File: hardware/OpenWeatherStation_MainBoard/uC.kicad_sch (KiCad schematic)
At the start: 1 part, among them U1 STM32F107VCTx

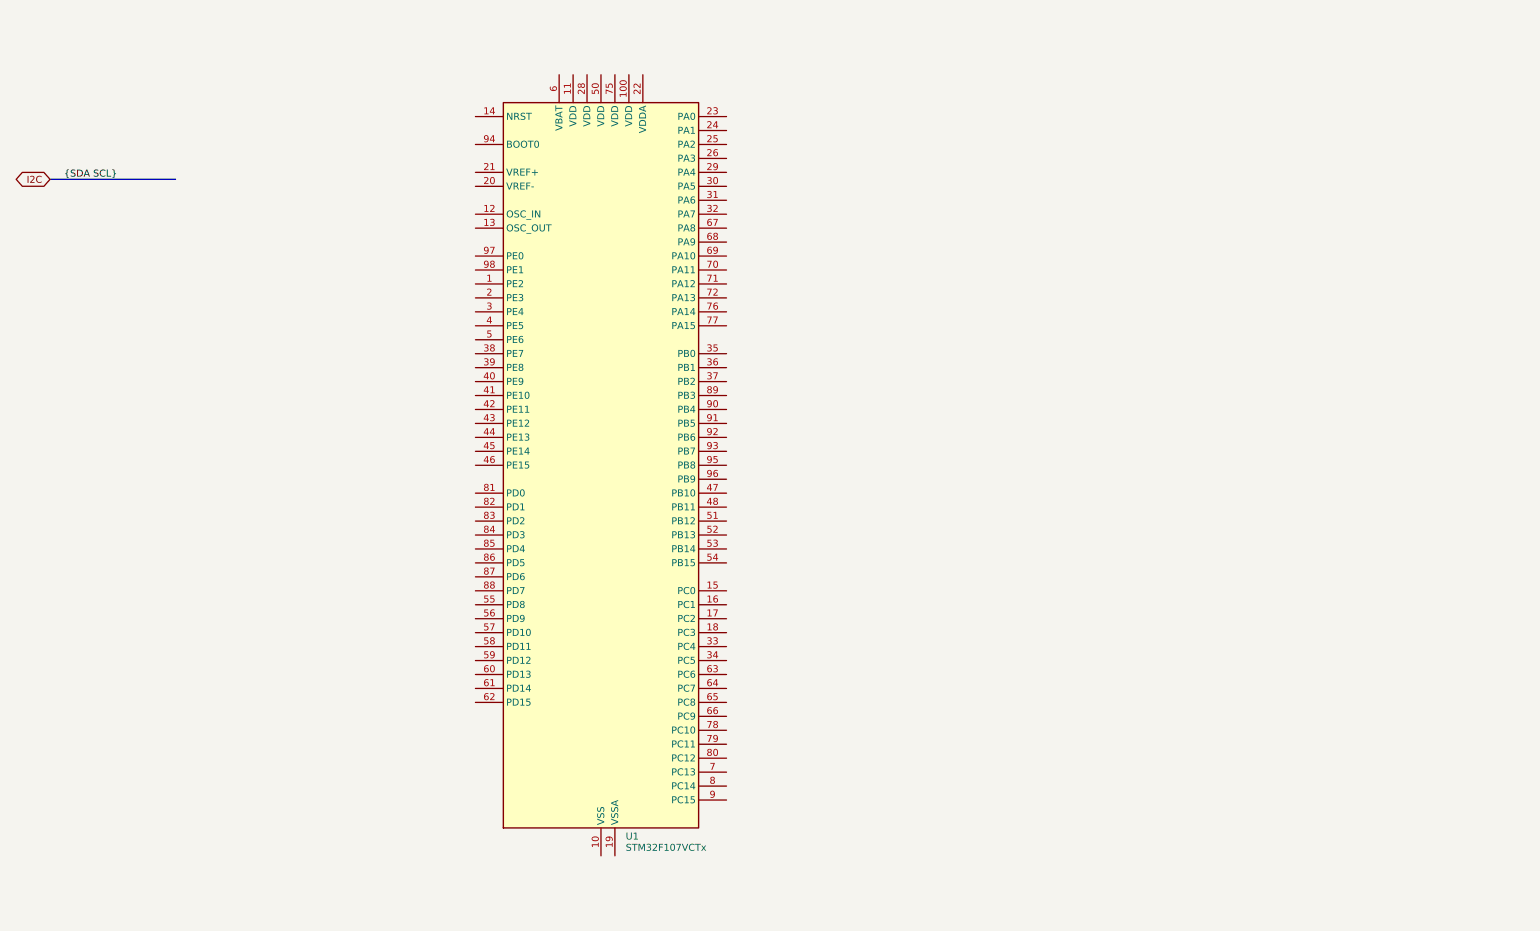
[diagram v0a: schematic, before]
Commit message: update board schematics (sensors, ethernet ...)
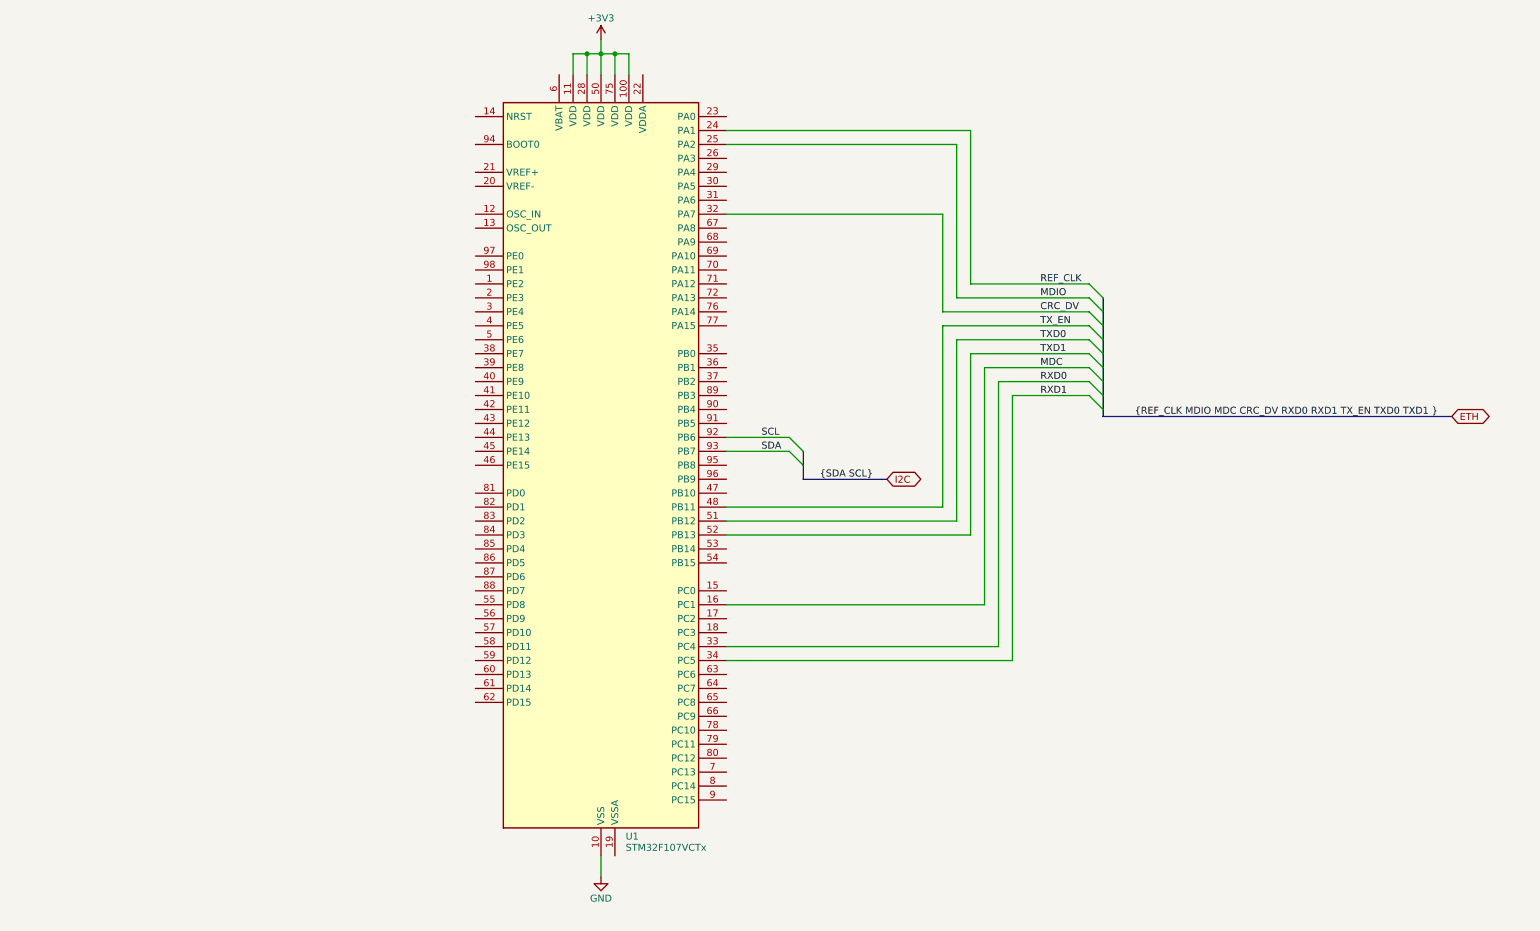
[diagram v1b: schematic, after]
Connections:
- net GND: now reaches U1.10 (VSS), U1.27 (VSS), U1.49 (VSS), U1.74 (VSS), U1.99 (VSS)
- net +3V3: now reaches U1.100 (VDD)
- net +3V3: now also U1.11 (VDD), U1.28 (VDD), U1.50 (VDD), U1.75 (VDD)
- net MDC: now reaches U1.16 (PC1)
- net REF_CLK: now reaches U1.24 (PA1)
- net MDIO: now reaches U1.25 (PA2)
- net CRC_DV: now reaches U1.32 (PA7)
- net RXD0: now reaches U1.33 (PC4)
- net RXD1: now reaches U1.34 (PC5)
- net TX_EN: now reaches U1.48 (PB11)
- net TXD0: now reaches U1.51 (PB12)
- net TXD1: now reaches U1.52 (PB13)
- net SCL: now reaches U1.92 (PB6)
- net SDA: now reaches U1.93 (PB7)

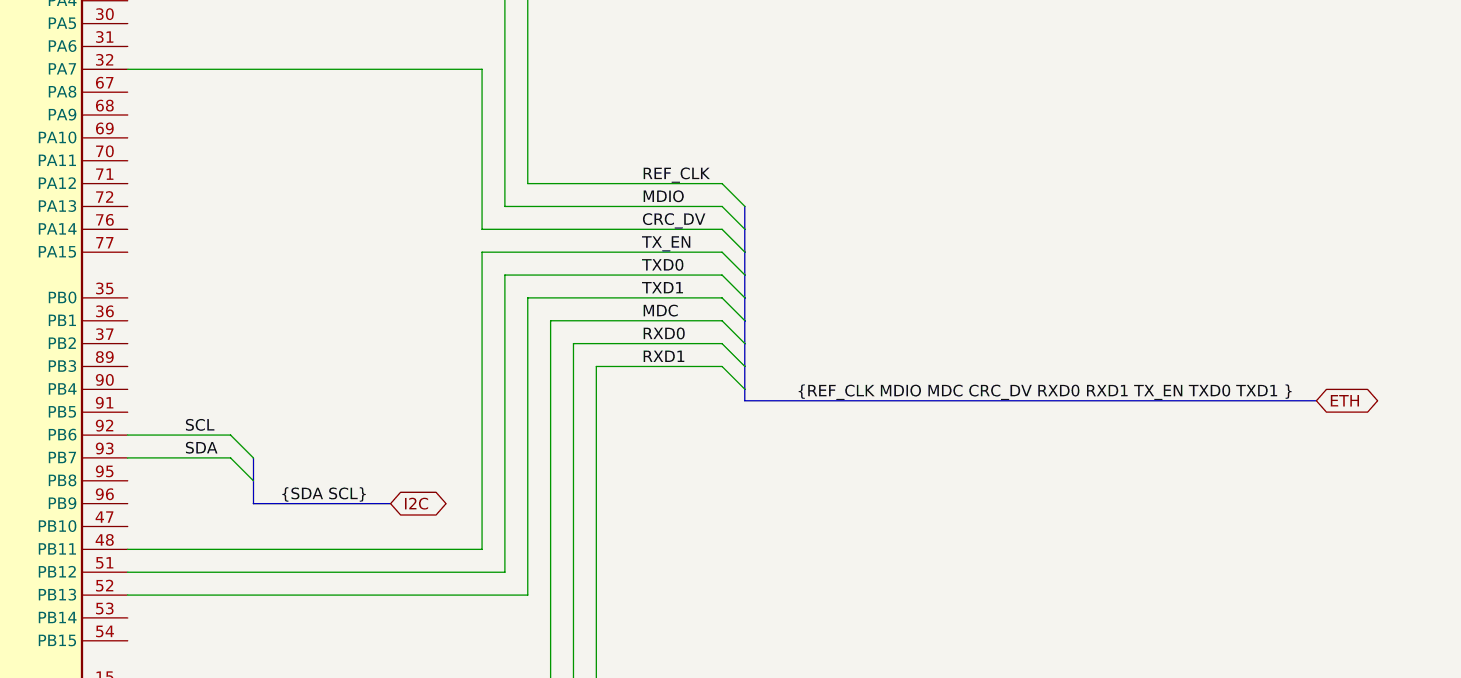
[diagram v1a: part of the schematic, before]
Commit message: fix hierarchical bus
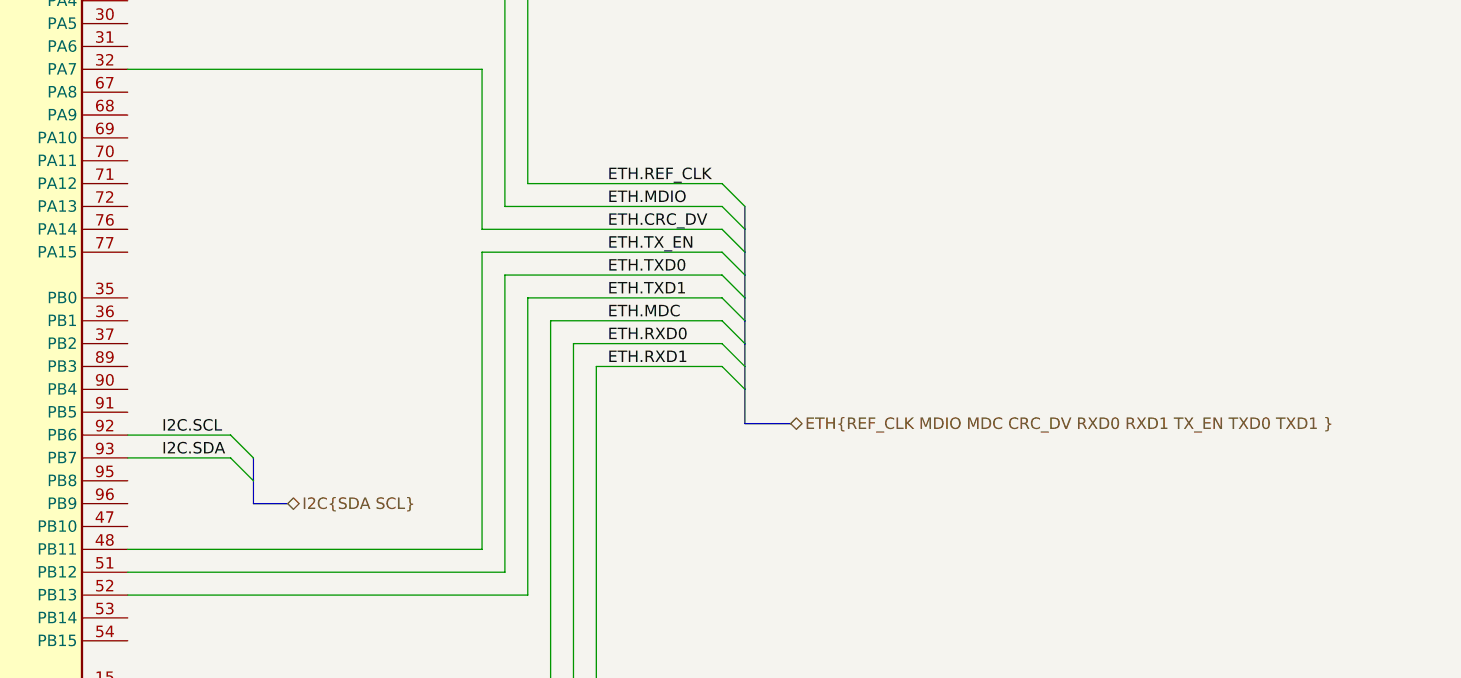
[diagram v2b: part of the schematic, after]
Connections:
- net CRC_DV renamed ETH.CRC_DV
- net MDC renamed ETH.MDC
- net MDIO renamed ETH.MDIO
- net REF_CLK renamed ETH.REF_CLK
- net RXD0 renamed ETH.RXD0
- net RXD1 renamed ETH.RXD1
- net SCL renamed I2C.SCL
- net SDA renamed I2C.SDA
- net TXD0 renamed ETH.TXD0
- net TXD1 renamed ETH.TXD1
- net TX_EN renamed ETH.TX_EN
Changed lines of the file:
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@@
+    (stroke (width 0) (type default))
+  )
+  (wire (pts (xy 196.85 86.36) (xy 210.82 86.36))
     (stroke (width 0) (type default))
   )
@@
     (stroke (width 0) (type default))
   )
-  (wire (pts (xy 186.69 76.2) (xy 210.82 76.2))
-    (stroke (width 0) (type default))
-  )
   (bus (pts (xy 213.36 73.66) (xy 213.36 76.2))
-    (stroke (width 0) (type default))
-  )
-  (wire (pts (xy 144.78 96.52) (xy 156.21 96.52))
     (stroke (width 0) (type default))
   )
@@
     (stroke (width 0) (type default))
   )
+  (bus (pts (xy 213.36 92.71) (xy 218.44 92.71))
+    (stroke (width 0) (type default))
+  )
   (wire (pts (xy 144.78 111.76) (xy 189.23 111.76))
+    (stroke (width 0) (type default))
+  )
+  (wire (pts (xy 184.15 71.12) (xy 210.82 71.12))
     (stroke (width 0) (type default))
   )
@@
     (stroke (width 0) (type default))
   )
-  (bus (pts (xy 213.36 86.36) (xy 213.36 88.9))
+  (wire (pts (xy 144.78 96.52) (xy 156.21 96.52))
     (stroke (width 0) (type default))
   )
-  (wire (pts (xy 184.15 71.12) (xy 210.82 71.12))
+  (bus (pts (xy 213.36 86.36) (xy 213.36 88.9))
     (stroke (width 0) (type default))
   )
@@
   )
   (bus (pts (xy 213.36 81.28) (xy 213.36 83.82))
-    (stroke (width 0) (type default))
-  )
-  (wire (pts (xy 144.78 93.98) (xy 156.21 93.98))
     (stroke (width 0) (type default))
   )
@@
     (stroke (width 0) (type default))
   )
-  (wire (pts (xy 184.15 73.66) (xy 210.82 73.66))
-    (stroke (width 0) (type default))
-  )
   (wire (pts (xy 184.15 71.12) (xy 184.15 53.34))
     (stroke (width 0) (type default))
@@
   )
   (wire (pts (xy 191.77 81.28) (xy 191.77 124.46))
-    (stroke (width 0) (type default))
-  )
-  (wire (pts (xy 196.85 86.36) (xy 210.82 86.36))
     (stroke (width 0) (type default))
   )
@@
     (stroke (width 0) (type default))
   )
-  (bus (pts (xy 158.75 101.6) (xy 173.99 101.6))
+  (wire (pts (xy 144.78 93.98) (xy 156.21 93.98))
+    (stroke (width 0) (type default))
+  )
+  (bus (pts (xy 158.75 101.6) (xy 162.56 101.6))
     (stroke (width 0) (type default))
   )
@@
     (stroke (width 0) (type default))
   )
-  (bus (pts (xy 213.36 90.17) (xy 213.36 88.9))
+  (bus (pts (xy 213.36 88.9) (xy 213.36 92.71))
+    (stroke (width 0) (type default))
+  )
+  (wire (pts (xy 184.15 73.66) (xy 210.82 73.66))
+    (stroke (width 0) (type default))
+  )
+  (wire (pts (xy 186.69 76.2) (xy 210.82 76.2))
     (stroke (width 0) (type default))
   )
@@
     (stroke (width 0) (type default))
   )
-  (bus (pts (xy 213.36 90.17) (xy 276.86 90.17))
-    (stroke (width 0) (type default))
-  )
-  (label "{SDA SCL}" (at 171.45 101.6 180) (fields_autoplaced)
-    (effects (font (size 1.27 1.27)) (justify right bottom))
-  )
-  (label "MDC" (at 201.93 81.28 0) (fields_autoplaced)
+  (label "ETH.MDC" (at 198.12 81.28 0) (fields_autoplaced)
     (effects (font (size 1.27 1.27)) (justify left bottom))
   )
-  (label "{REF_CLK MDIO MDC CRC_DV RXD0 RXD1 TX_EN TXD0 TXD1 }"
-    (at 274.32 90.17 180) (fields_autoplaced)
-    (effects (font (size 1.27 1.27)) (justify right bottom))
-  )
-  (label "SCL" (at 151.13 93.98 0) (fields_autoplaced)
+  (label "I2C.SCL" (at 148.59 93.98 0) (fields_autoplaced)
     (effects (font (size 1.27 1.27)) (justify left bottom))
   )
-  (label "CRC_DV" (at 201.93 71.12 0) (fields_autoplaced)
+  (label "ETH.CRC_DV" (at 198.12 71.12 0) (fields_autoplaced)
     (effects (font (size 1.27 1.27)) (justify left bottom))
   )
-  (label "TX_EN" (at 201.93 73.66 0) (fields_autoplaced)
+  (label "ETH.TX_EN" (at 198.12 73.66 0) (fields_autoplaced)
     (effects (font (size 1.27 1.27)) (justify left bottom))
   )
-  (label "TXD1" (at 201.93 78.74 0) (fields_autoplaced)
+  (label "ETH.TXD1" (at 198.12 78.74 0) (fields_autoplaced)
     (effects (font (size 1.27 1.27)) (justify left bottom))
   )
-  (label "SDA" (at 151.13 96.52 0) (fields_autoplaced)
+  (label "I2C.SDA" (at 148.59 96.52 0) (fields_autoplaced)
     (effects (font (size 1.27 1.27)) (justify left bottom))
   )
-  (label "REF_CLK" (at 201.93 66.04 0) (fields_autoplaced)
+  (label "ETH.REF_CLK" (at 198.12 66.04 0) (fields_autoplaced)
     (effects (font (size 1.27 1.27)) (justify left bottom))
   )
-  (label "RXD0" (at 201.93 83.82 0) (fields_autoplaced)
+  (label "ETH.RXD0" (at 198.12 83.82 0) (fields_autoplaced)
     (effects (font (size 1.27 1.27)) (justify left bottom))
   )
-  (label "TXD0" (at 201.93 76.2 0) (fields_autoplaced)
+  (label "ETH.TXD0" (at 198.12 76.2 0) (fields_autoplaced)
     (effects (font (size 1.27 1.27)) (justify left bottom))
   )
-  (label "MDIO" (at 201.93 68.58 0) (fields_autoplaced)
+  (label "ETH.MDIO" (at 198.12 68.58 0) (fields_autoplaced)
     (effects (font (size 1.27 1.27)) (justify left bottom))
   )
-  (label "RXD1" (at 201.93 86.36 0) (fields_autoplaced)
+  (label "ETH.RXD1" (at 198.12 86.36 0) (fields_autoplaced)
     (effects (font (size 1.27 1.27)) (justify left bottom))
   )
-  (global_label "ETH" (shape bidirectional) (at 276.86 90.17 0) (fields_autoplaced)
+  (hierarchical_label "ETH{REF_CLK MDIO MDC CRC_DV RXD0 RXD1 TX_EN TXD0 TXD1 }" (shape bidirectional)
+    (at 218.44 92.71 0) (fields_autoplaced)
     (effects (font (size 1.27 1.27)) (justify left))
-    (property "Intersheetrefs" "${INTERSHEET_REFS}" (at 283.5906 90.17 0)
-      (effects (font (size 1.27 1.27)) (justify left) hide)
-    )
   )
-  (global_label "I2C" (shape bidirectional) (at 173.99 101.6 0) (fields_autoplaced)
+  (hierarchical_label "I2C{SDA SCL}" (shape bidirectional) (at 162.56 101.6 0) (fields_autoplaced)
     (effects (font (size 1.27 1.27)) (justify left))
-    (property "Intersheetrefs" "${INTERSHEET_REFS}" (at 180.2784 101.6 0)
-      (effects (font (size 1.27 1.27)) (justify left) hide)
-    )
   )
   (symbol (lib_id "power:GND") (at 121.92 173.99 0) (unit 1)
